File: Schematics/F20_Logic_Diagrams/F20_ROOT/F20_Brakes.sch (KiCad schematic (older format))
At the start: 1 part

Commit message: Updated Brakes diagram. Updated power management diagram. Updated relevant library symbols. Updated README.
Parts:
- added U?: Brake_Light_Switch, symbol FSAE_Library:Brake_Light_Switch
- added U? (x2): Brake_Pressure_Sensor, symbol FSAE_Library:Brake_Pressure_Sensor
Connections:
- net labels added: ECU_5V, ECU_AGND, ECU_BL, ECU_BL_SW, ECU_FBPS, ECU_RBPS
- net labels removed: ECU_Brake_Light
- wire segments 3 -> 16
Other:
- note added: "Front"
- note added: "Rear"
- moved on the sheet: U?
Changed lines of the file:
@@
 $Descr A 11000 8500
 encoding utf-8
-Sheet 6 6
+Sheet 5 7
 Title "Brakes"
 Date "2020-01-28"
@@
 Comp "F20"
 Comment1 "Alex Domagala"
-Comment2 ""
+Comment2 "Cristian Valadez"
 Comment3 ""
 Comment4 ""
 $EndDescr
-Wire Wire Line
-	7000 1750 3500 1750
-$Comp
-L power:GND #PWR?
-U 1 1 5E2E5218
-P 3500 2000
-F 0 "#PWR?" H 3500 1750 50  0001 C CNN
-F 1 "GND" H 3505 1827 50  0000 C CNN
-F 2 "" H 3500 2000 50  0001 C CNN
-F 3 "" H 3500 2000 50  0001 C CNN
-	1    3500 2000
-	1    0    0    -1
-$EndComp
-Text GLabel 3500 1500 0    50   Input ~ 0
-ECU_Brake_Light
-Wire Wire Line
-	7000 1500 3500 1500
+Text GLabel 2500 5000 0    50   Input ~ 0
+ECU_BL
 $Comp
 L FSAE_Library:Brake_Light U?
 U 1 1 5E30D69C
-P 7000 1500
-F 0 "U?" H 7250 1650 50  0000 L CNN
-F 1 "Brake_Light" H 7150 1550 50  0001 C CNN
-F 2 "" H 7500 2000 50  0001 C CNN
-F 3 "" H 7500 2000 50  0001 C CNN
-	1    7000 1500
+P 8550 5000
+F 0 "U?" H 8800 5150 50  0000 L CNN
+F 1 "Brake_Light" H 8700 5050 50  0001 C CNN
+F 2 "" H 9050 5500 50  0001 C CNN
+F 3 "" H 9050 5500 50  0001 C CNN
+	1    8550 5000
+	1    0    0    -1
+$EndComp
+$Comp
+L FSAE_Library:Brake_Light_Switch U?
+U 1 1 5E324B1C
+P 8550 4000
+F 0 "U?" H 9078 3850 50  0000 L CNN
+F 1 "Brake_Light_Switch" H 8700 4050 50  0001 C CNN
+F 2 "" H 9050 4500 50  0001 C CNN
+F 3 "" H 9050 4500 50  0001 C CNN
+	1    8550 4000
+	1    0    0    -1
+$EndComp
+$Comp
+L FSAE_Library:Brake_Pressure_Sensor U?
+U 1 1 5E325994
+P 8550 2000
+F 0 "U?" H 9078 1750 50  0000 L CNN
+F 1 "Brake_Pressure_Sensor" H 8700 2050 50  0001 C CNN
+F 2 "" H 9050 2500 50  0001 C CNN
+F 3 "" H 9050 2500 50  0001 C CNN
+	1    8550 2000
+	1    0    0    -1
+$EndComp
+$Comp
+L FSAE_Library:Brake_Pressure_Sensor U?
+U 1 1 5E326371
+P 8550 3000
+F 0 "U?" H 9078 2750 50  0000 L CNN
+F 1 "Brake_Pressure_Sensor" H 8700 3050 50  0001 C CNN
+F 2 "" H 9050 3500 50  0001 C CNN
+F 3 "" H 9050 3500 50  0001 C CNN
+	1    8550 3000
 	1    0    0    -1
 $EndComp
 Wire Wire Line
-	3500 1750 3500 2000
+	8550 2500 6500 2500
+Wire Wire Line
+	6500 2500 6500 3500
+Wire Wire Line
+	8550 3500 6500 3500
+Wire Wire Line
+	8550 4250 8000 4250
+Wire Wire Line
+	8000 4250 8000 5250
+Wire Wire Line
+	8550 5250 8000 5250
+Connection ~ 8000 5250
+Wire Wire Line
+	8000 5250 8000 5500
+Text GLabel 2500 2000 0    50   Output ~ 0
+ECU_FBPS
+Text GLabel 2500 2250 0    50   Input ~ 0
+ECU_5V
+Wire Wire Line
+	2500 2000 8550 2000
+Wire Wire Line
+	2500 2250 6750 2250
+Wire Wire Line
+	2500 3000 8550 3000
+Text GLabel 2500 2500 0    50   Input ~ 0
+ECU_AGND
+Text GLabel 2500 3000 0    50   Output ~ 0
+ECU_RBPS
+Wire Wire Line
+	6500 2500 2500 2500
+Connection ~ 6500 2500
+Wire Wire Line
+	8550 3250 6750 3250
+Wire Wire Line
+	6750 3250 6750 2250
+Connection ~ 6750 2250
+Wire Wire Line
+	6750 2250 8550 2250
+Wire Wire Line
+	2500 4000 8550 4000
+Text GLabel 2500 4000 0    50   Output ~ 0
+ECU_BL_SW
+Wire Wire Line
+	8550 5000 2500 5000
+Text Notes 8920 2960 0    33   ~ 0
+Rear
+Text Notes 8900 1970 0    33   ~ 0
+Front
+$Comp
+L power:GND #PWR?
+U 1 1 5E479A01
+P 8000 5500
+F 0 "#PWR?" H 8000 5250 50  0001 C CNN
+F 1 "GND" H 8005 5327 50  0000 C CNN
+F 2 "" H 8000 5500 50  0001 C CNN
+F 3 "" H 8000 5500 50  0001 C CNN
+	1    8000 5500
+	1    0    0    -1
+$EndComp
 $EndSCHEMATC

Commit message: Added GND and GND_CHASSIS symbols, updated relevant schematics. Restructured Powertrain hierarchy. Created ECU Connector symbols.
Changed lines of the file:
@@
 $Descr A 11000 8500
 encoding utf-8
-Sheet 5 7
+Sheet 4 7
 Title "Brakes"
-Date "2020-01-28"
-Rev "A"
+Date "2020-02-03"
+Rev "B"
 Comp "F20"
 Comment1 "Alex Domagala"
@@
 Front
 $Comp
-L power:GND #PWR?
-U 1 1 5E479A01
+L FSAE_Library:GND #PWR?
+U 1 1 5E3C206F
 P 8000 5500
-F 0 "#PWR?" H 8000 5250 50  0001 C CNN
-F 1 "GND" H 8005 5327 50  0000 C CNN
-F 2 "" H 8000 5500 50  0001 C CNN
-F 3 "" H 8000 5500 50  0001 C CNN
+F 0 "#PWR?" H 8000 5300 50  0001 C CNN
+F 1 "GND" H 8004 5346 50  0000 C CNN
+F 2 "" H 8000 5450 50  0001 C CNN
+F 3 "" H 8000 5450 50  0001 C CNN
 	1    8000 5500
 	1    0    0    -1

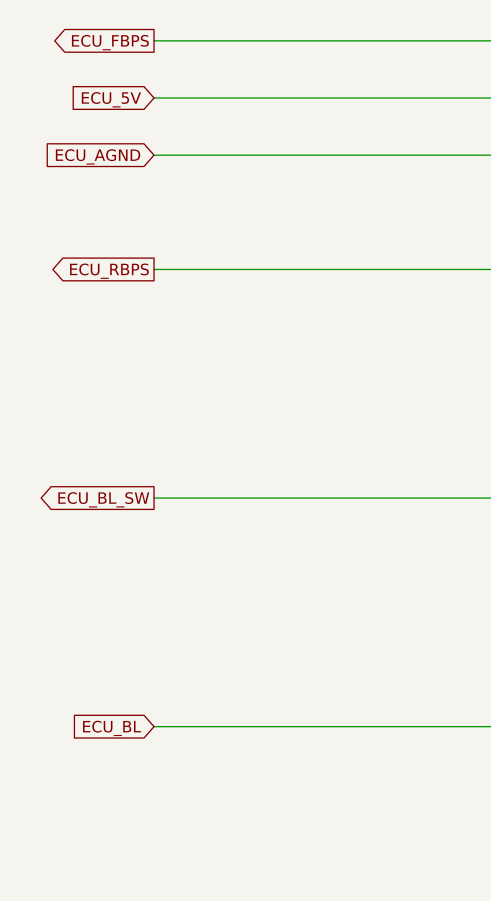
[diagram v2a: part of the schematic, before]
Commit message: Updated per AD commit. O2 sensor schematic, transponder schematic.
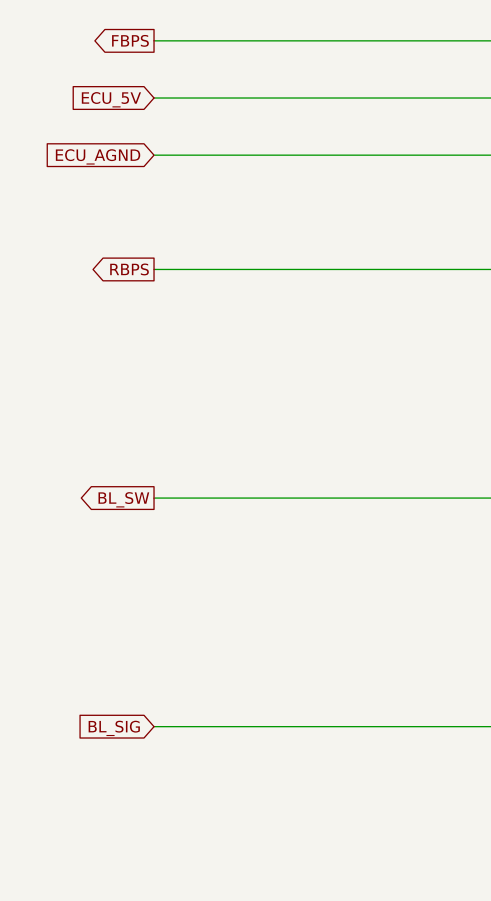
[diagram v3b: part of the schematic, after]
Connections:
- net ECU_BL renamed BL_SIG
- net ECU_BL_SW renamed BL_SW
- net ECU_FBPS renamed FBPS
- net ECU_RBPS renamed RBPS
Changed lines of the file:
@@
 EESchema Schematic File Version 4
-LIBS:F20_ROOT-cache
 EELAYER 30 0
 EELAYER END
 $Descr A 11000 8500
 encoding utf-8
-Sheet 4 7
+Sheet 6 9
 Title "Brakes"
 Date "2020-02-03"
@@
 $EndDescr
 Text GLabel 2500 5000 0    50   Input ~ 0
-ECU_BL
+BL_SIG
 $Comp
 L FSAE_Library:Brake_Light U?
@@
 Wire Wire Line
 	8000 5250 8000 5500
-Text GLabel 2500 2000 0    50   Output ~ 0
-ECU_FBPS
 Text GLabel 2500 2250 0    50   Input ~ 0
 ECU_5V
@@
 ECU_AGND
 Text GLabel 2500 3000 0    50   Output ~ 0
-ECU_RBPS
+RBPS
 Wire Wire Line
 	6500 2500 2500 2500
@@
 	2500 4000 8550 4000
 Text GLabel 2500 4000 0    50   Output ~ 0
-ECU_BL_SW
+BL_SW
 Wire Wire Line
 	8550 5000 2500 5000
@@
 	1    0    0    -1
 $EndComp
+Text GLabel 2500 2000 0    50   Output ~ 0
+FBPS
 $EndSCHEMATC

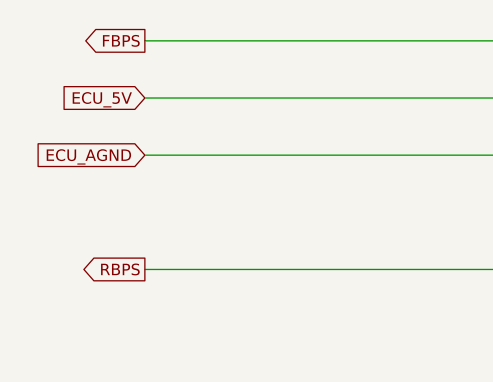
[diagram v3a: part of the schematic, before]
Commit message: Weekly update. Added Tire temp sensors drawing.
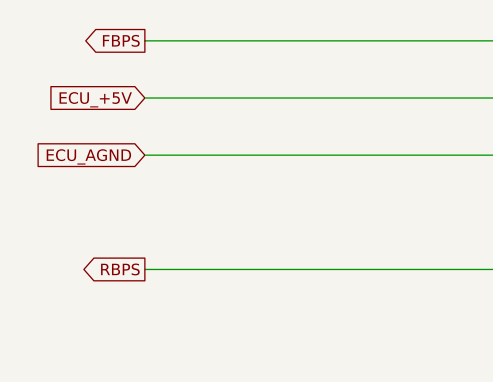
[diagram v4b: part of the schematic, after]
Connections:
- net ECU_5V renamed ECU_+5V
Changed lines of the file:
@@
 EESchema Schematic File Version 4
+LIBS:F20_ROOT-cache
 EELAYER 30 0
 EELAYER END
 $Descr A 11000 8500
 encoding utf-8
-Sheet 6 9
+Sheet 7 11
 Title "Brakes"
 Date "2020-02-03"
@@
 	8000 5250 8000 5500
 Text GLabel 2500 2250 0    50   Input ~ 0
-ECU_5V
+ECU_+5V
 Wire Wire Line
 	2500 2000 8550 2000
@@
 Front
 $Comp
-L FSAE_Library:GND #PWR?
+L FSAE_Library:GND #PWR0105
 U 1 1 5E3C206F
 P 8000 5500
-F 0 "#PWR?" H 8000 5300 50  0001 C CNN
+F 0 "#PWR0105" H 8000 5300 50  0001 C CNN
 F 1 "GND" H 8004 5346 50  0000 C CNN
 F 2 "" H 8000 5450 50  0001 C CNN

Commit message: 02/18/20 update
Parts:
- gave numbers to parts that had none: 4
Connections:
- net ECU_+5V renamed ECU_+5V_1
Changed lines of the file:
@@
 $Descr A 11000 8500
 encoding utf-8
-Sheet 7 11
+Sheet 7 13
 Title "Brakes"
 Date "2020-02-03"
@@
 BL_SIG
 $Comp
-L FSAE_Library:Brake_Light U?
+L FSAE_Library:Brake_Light U10
 U 1 1 5E30D69C
 P 8550 5000
-F 0 "U?" H 8800 5150 50  0000 L CNN
+F 0 "U10" H 8800 5150 50  0000 L CNN
 F 1 "Brake_Light" H 8700 5050 50  0001 C CNN
 F 2 "" H 9050 5500 50  0001 C CNN
@@
 $EndComp
 $Comp
-L FSAE_Library:Brake_Light_Switch U?
+L FSAE_Library:Brake_Light_Switch U9
 U 1 1 5E324B1C
 P 8550 4000
-F 0 "U?" H 9078 3850 50  0000 L CNN
+F 0 "U9" H 9078 3850 50  0000 L CNN
 F 1 "Brake_Light_Switch" H 8700 4050 50  0001 C CNN
 F 2 "" H 9050 4500 50  0001 C CNN
@@
 $EndComp
 $Comp
-L FSAE_Library:Brake_Pressure_Sensor U?
+L FSAE_Library:Brake_Pressure_Sensor U7
 U 1 1 5E325994
 P 8550 2000
-F 0 "U?" H 9078 1750 50  0000 L CNN
+F 0 "U7" H 9078 1750 50  0000 L CNN
 F 1 "Brake_Pressure_Sensor" H 8700 2050 50  0001 C CNN
 F 2 "" H 9050 2500 50  0001 C CNN
@@
 $EndComp
 $Comp
-L FSAE_Library:Brake_Pressure_Sensor U?
+L FSAE_Library:Brake_Pressure_Sensor U8
 U 1 1 5E326371
 P 8550 3000
-F 0 "U?" H 9078 2750 50  0000 L CNN
+F 0 "U8" H 9078 2750 50  0000 L CNN
 F 1 "Brake_Pressure_Sensor" H 8700 3050 50  0001 C CNN
 F 2 "" H 9050 3500 50  0001 C CNN
@@
 Wire Wire Line
 	8000 5250 8000 5500
-Text GLabel 2500 2250 0    50   Input ~ 0
-ECU_+5V
 Wire Wire Line
 	2500 2000 8550 2000
@@
 Front
 $Comp
-L FSAE_Library:GND #PWR0105
+L FSAE_Library:GND #PWR08
 U 1 1 5E3C206F
 P 8000 5500
-F 0 "#PWR0105" H 8000 5300 50  0001 C CNN
+F 0 "#PWR08" H 8000 5300 50  0001 C CNN
 F 1 "GND" H 8004 5346 50  0000 C CNN
 F 2 "" H 8000 5450 50  0001 C CNN
@@
 Text GLabel 2500 2000 0    50   Output ~ 0
 FBPS
+Text GLabel 2500 2250 0    50   Input ~ 0
+ECU_+5V_1
 $EndSCHEMATC

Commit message: 02/19/20 update
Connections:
- net ECU_AGND renamed ECU_AGND_1
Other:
- note added: "BL : Brake Light\nFBPS : Front Brake Pressure Sensor\nRBPS : Rear Brake Pressure Sensor"
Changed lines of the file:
@@
 $Descr A 11000 8500
 encoding utf-8
-Sheet 7 13
+Sheet 8 13
 Title "Brakes"
 Date "2020-02-03"
@@
 Wire Wire Line
 	2500 3000 8550 3000
-Text GLabel 2500 2500 0    50   Input ~ 0
-ECU_AGND
 Text GLabel 2500 3000 0    50   Output ~ 0
 RBPS
@@
 Text GLabel 2500 2250 0    50   Input ~ 0
 ECU_+5V_1
+Text Notes 4850 7250 0    50   ~ 0
+BL : Brake Light\nFBPS : Front Brake Pressure Sensor\nRBPS : Rear Brake Pressure Sensor
+Wire Notes Line
+	6250 7000 4800 7000
+Wire Notes Line
+	4800 7000 4800 7300
+Wire Notes Line
+	4800 7300 6250 7300
+Text GLabel 2500 2500 0    50   Input ~ 0
+ECU_AGND_1
 $EndSCHEMATC
